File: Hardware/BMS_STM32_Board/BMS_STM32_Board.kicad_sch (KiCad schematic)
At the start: 0 parts

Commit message: hardware schematic
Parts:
- added C1, C2, C3, C4: 100nF, symbol Device:C_Small
- added C5: 4.7uF, symbol Device:C_Small
- added U1: STM32F103C8Tx, Package_QFP:LQFP-48_7x7mm_P0.5mm, symbol MCU_ST_STM32F1:STM32F103C8Tx
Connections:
- new net: U1.23 (VSS), U1.35 (VSS), U1.47 (VSS)
- new net +3V3: C1.1, C2.1, C3.1, C4.1, C5.1
- new net GND: C1.2, C2.2, C3.2, C4.2, C5.2

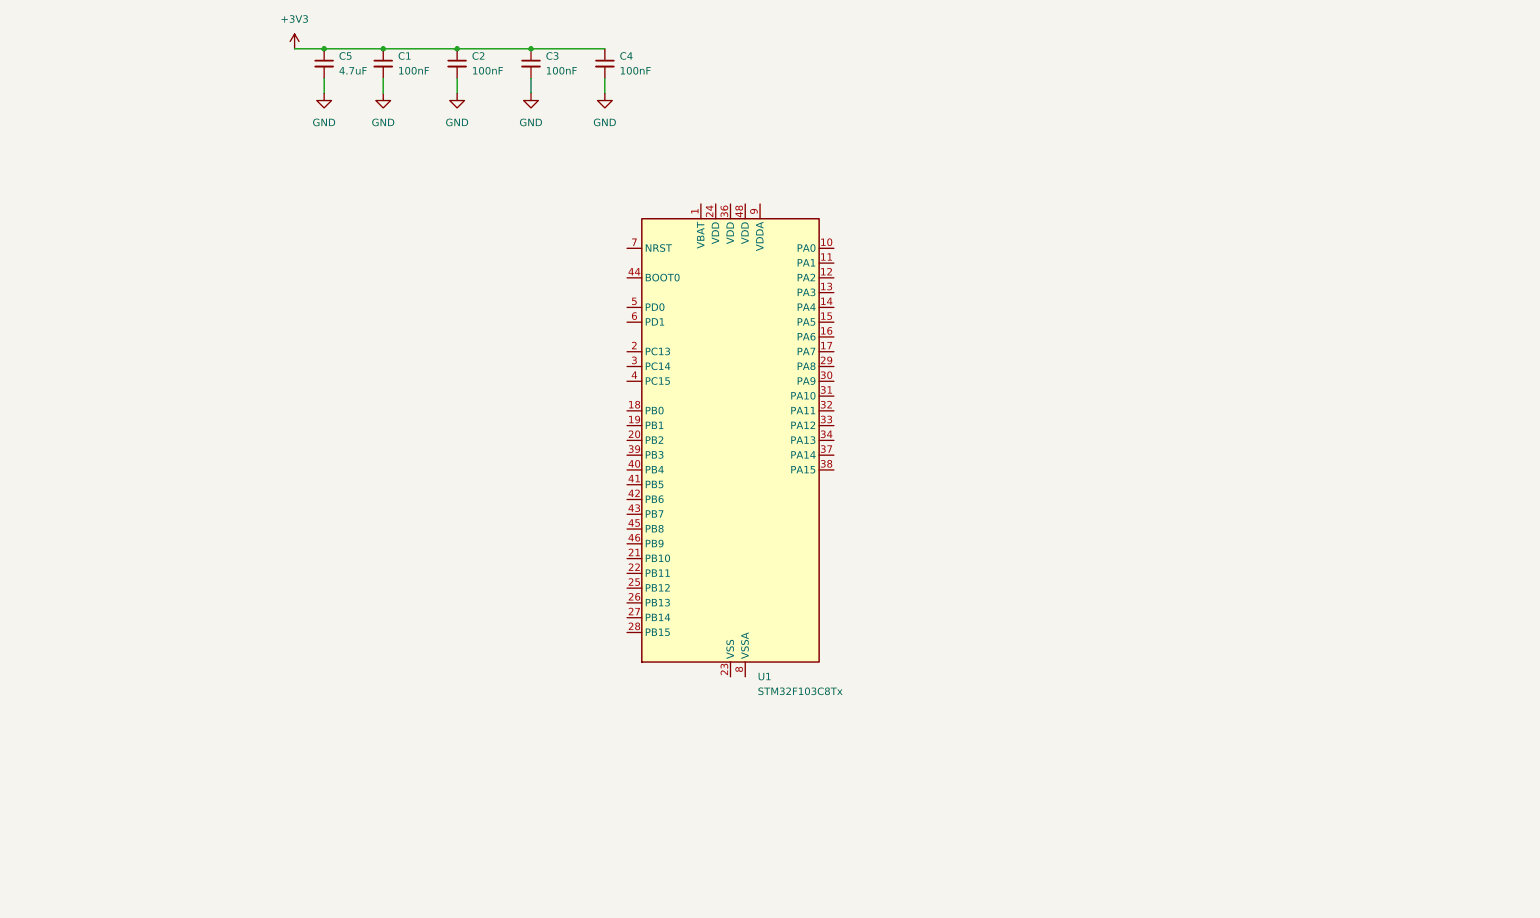
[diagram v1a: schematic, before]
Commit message: Current Sense Schematic
The current sense schematic was added the bms_stm32_board.
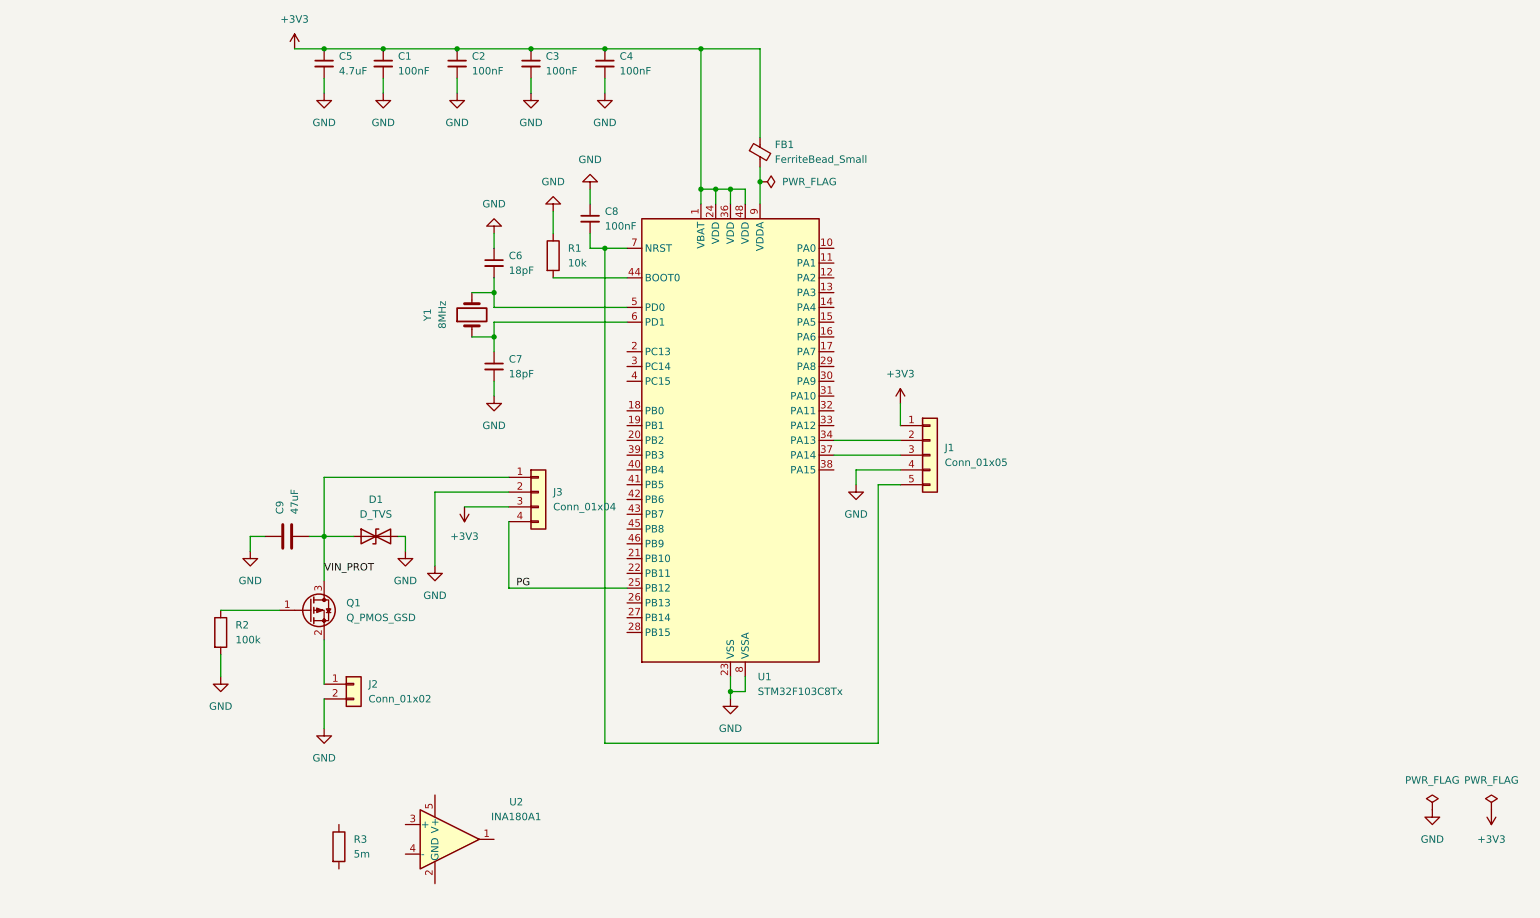
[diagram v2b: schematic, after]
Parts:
- added C6, C7: 18pF, symbol Device:C_Small
- added C8: 100nF, symbol Device:C_Small
- added C9: 47uF, symbol Device:C
- added D1: D_TVS, symbol Device:D_TVS
- added FB1: FerriteBead_Small, symbol Device:FerriteBead_Small
- added J1: Conn_01x05, symbol Connector_Generic:Conn_01x05
- added J2: Conn_01x02, symbol Connector_Generic:Conn_01x02
- added J3: Conn_01x04, symbol Connector_Generic:Conn_01x04
- added Q1: Q_PMOS_GSD, symbol Transistor_FET:Q_PMOS_GSD
- added R1: 10k, symbol Device:R
- added R2: 100k, symbol Device:R
- added R3: 5m, symbol Device:R
- added U2: INA180A1, Package_TO_SOT_SMD:SOT-23-5, symbol Amplifier_Current:INA180A1
- added Y1: 8MHz, symbol Device:Crystal
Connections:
- net +3V3: now also U1.1 (VBAT), U1.24 (VDD), U1.36 (VDD), U1.48 (VDD), FB1.1, J1.1 (Pin_1), J3.3 (Pin_3)
- net GND: now also U1.23 (VSS), U1.35 (VSS), U1.47 (VSS), U1.8 (VSSA), C6.1, C7.2, C8.1, C9.1, D1.2 (A2), J1.4 (Pin_4), J2.2 (Pin_2), J3.2 (Pin_2), R1.1, R2.2
- net PG: now reaches U1.25 (PB12)
- net PG: now also J3.4 (Pin_4)
- net at U1.34 (PA13): now also J1.2 (Pin_2)
- net at U1.37 (PA14): now also J1.3 (Pin_3)
- net at U1.44 (BOOT0): now also R1.2
- net at U1.5 (PD0): now also C6.2, Y1.2
- net at U1.6 (PD1): now also C7.1, Y1.1
- net at U1.7 (NRST): now also C8.2, J1.5 (Pin_5)
- net at U1.9 (VDDA): now also FB1.2
- new net: Q1.1 (G), R2.1
- new net: J2.1 (Pin_1), Q1.2 (S)
- new net VIN_PROT: C9.2, D1.1 (A1), J3.1 (Pin_1), Q1.3 (D)

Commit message: current sense
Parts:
- removed U2: INA180A1, Package_TO_SOT_SMD:SOT-23-5, symbol Amplifier_Current:INA180A1
- added C10, C11, C12: 100nF, symbol Device:C_Small
- added J4: Conn_01x02, symbol Connector_Generic:Conn_01x02
- added R4, R5: 10k, symbol Device:R
- added R6: 1k, symbol Device:R
- added U3: INA181, Package_TO_SOT_SMD:SOT-23-6, symbol Amplifier_Current:INA181
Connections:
- net +3V3: now also C10.1, R5.1, U3.6 (V+)
- net GND: now also C10.2, C11.1, C12.2, J4.2 (Pin_2), R4.2, U3.2 (GND)
- net VIN_PROT: now also R3.2, U3.4 (-)
- net LOAD+: now reaches R3.1
- net LOAD+: now also J4.1 (Pin_1), U3.3 (+)
- net at U1.18 (PB0): now also C11.2, R6.1
- new net: C12.1, R4.1, R5.2, U3.5 (REF)
- new net: R6.2, U3.1
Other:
- moved on the sheet: C6, C7, R1, R3, Y1

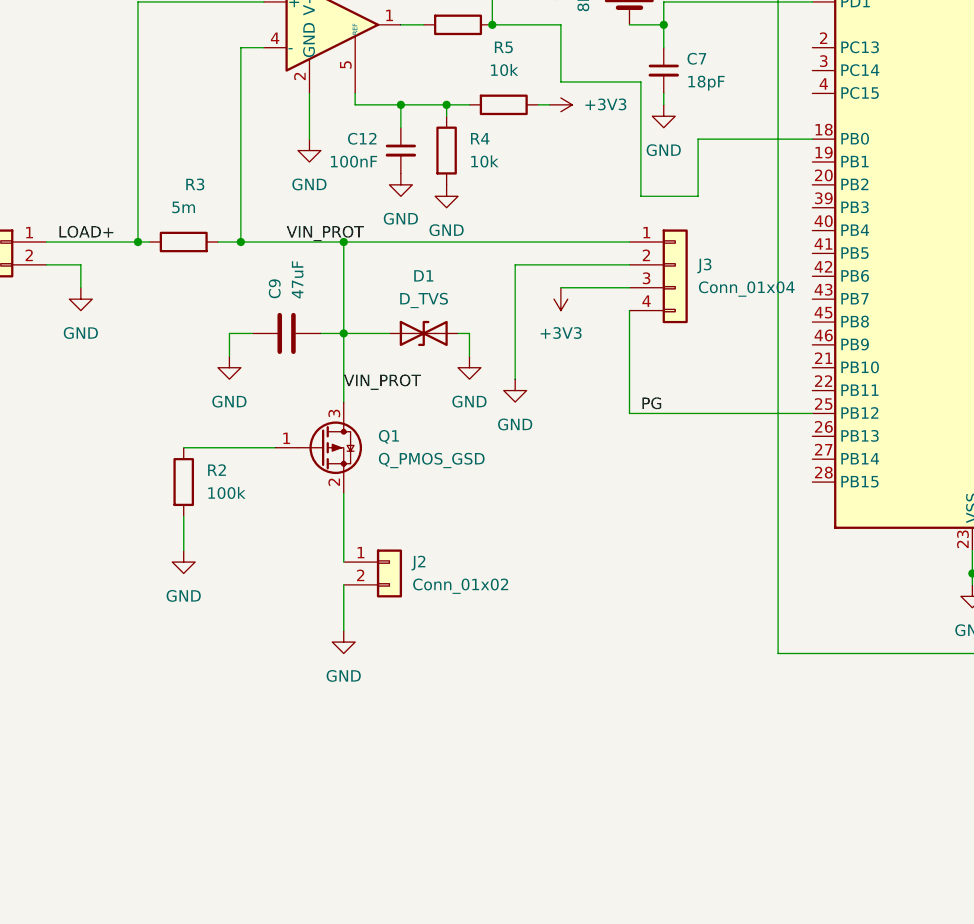
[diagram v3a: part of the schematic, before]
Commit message: Hardware: voltage sense divider (33k/10k + 100nF) to PB1, ERC clean
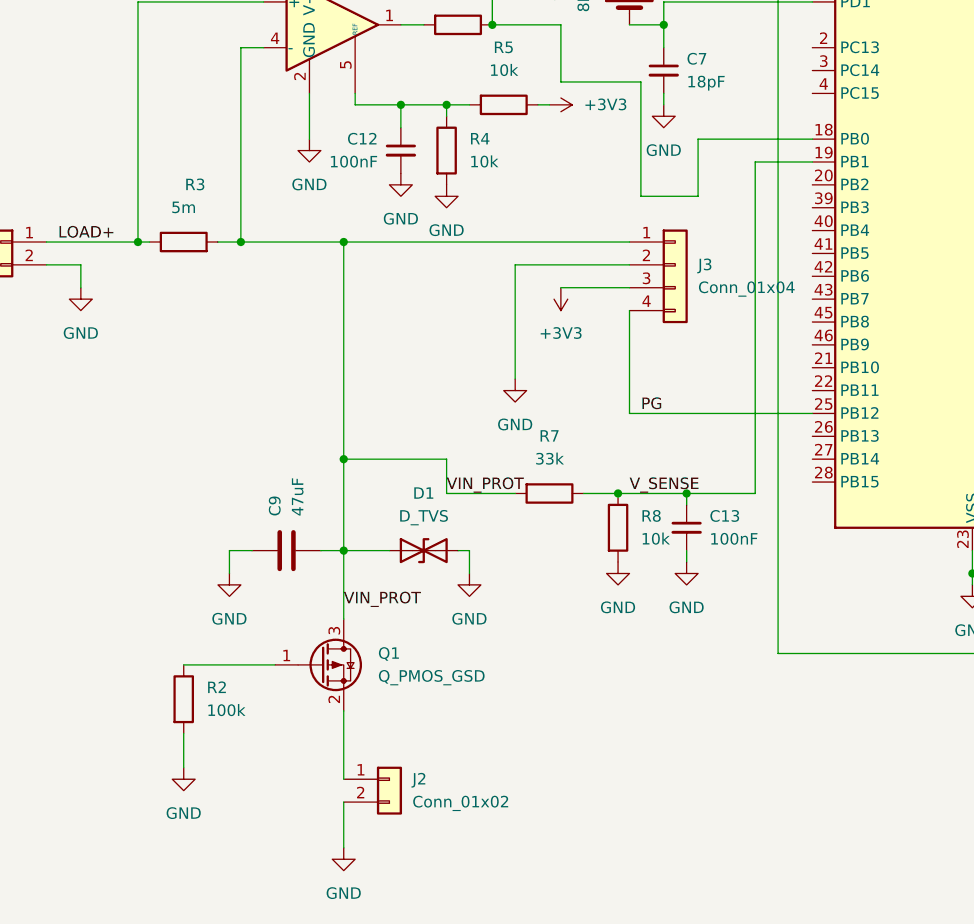
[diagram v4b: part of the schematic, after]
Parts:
- added C13: 100nF, symbol Device:C_Small
- added R7: 33k, symbol Device:R
- added R8: 10k, symbol Device:R
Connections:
- net GND: now also C13.2, R8.2
- net VIN_PROT: now also R7.2
- net V_SENSE: now reaches U1.19 (PB1)
- net V_SENSE: now also C13.1, R7.1, R8.1
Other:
- moved on the sheet: C9, D1, J2, Q1, R2

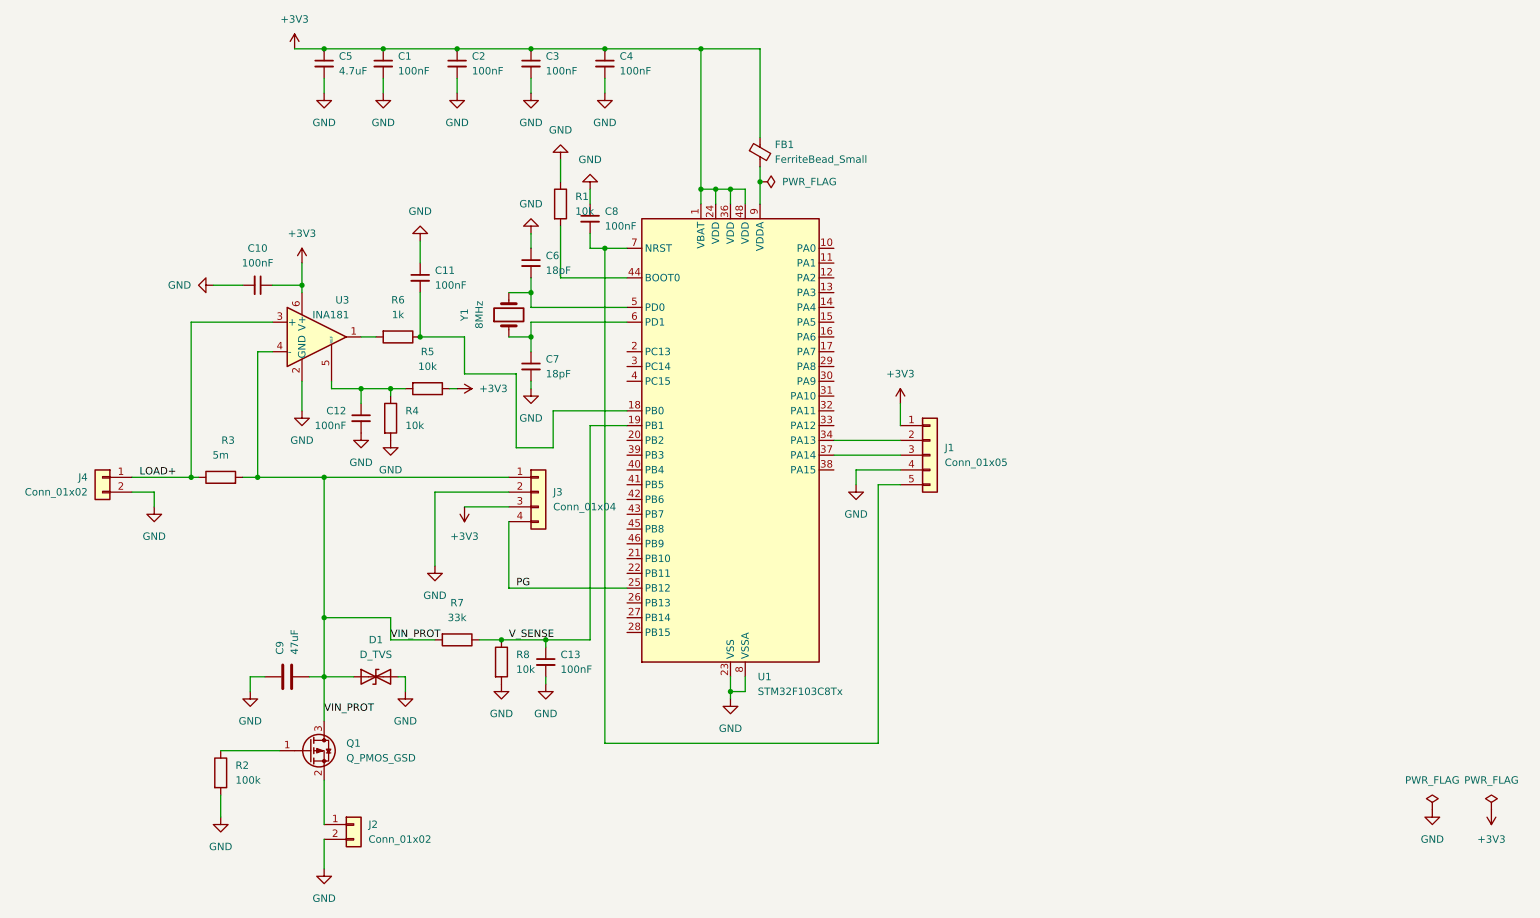
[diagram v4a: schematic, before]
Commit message: Hardware: TM1637 display block + LED indicators, ERC clean
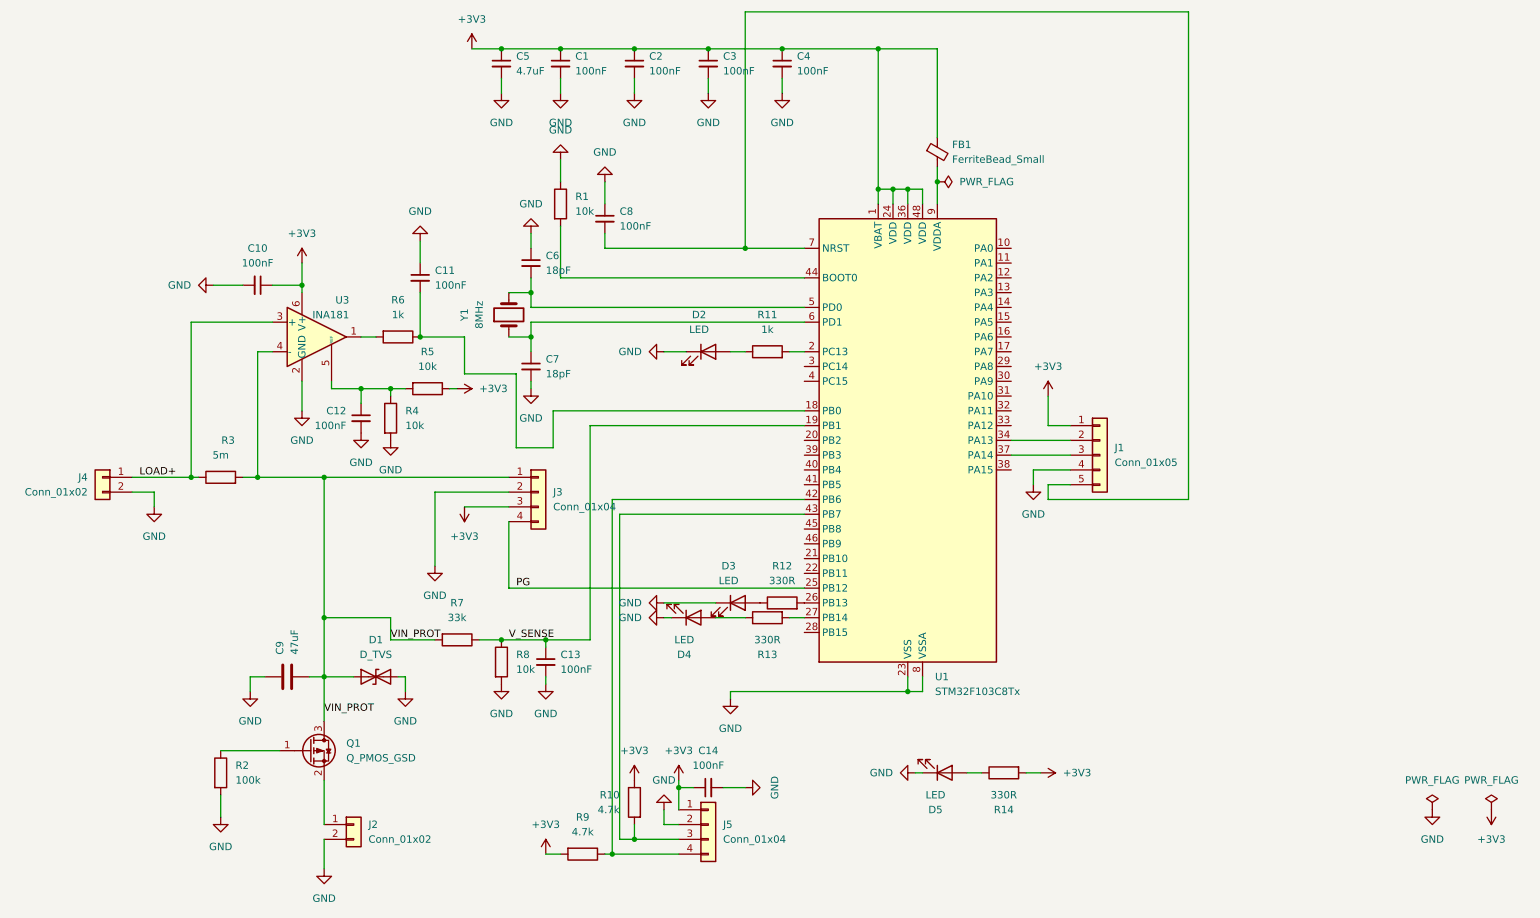
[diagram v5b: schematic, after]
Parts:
- added C14: 100nF, symbol Device:C_Small
- added D2, D3, D4, D5: LED, symbol Device:LED
- added J5: Conn_01x04, symbol Connector_Generic:Conn_01x04
- added R10, R9: 4.7k, symbol Device:R
- added R11: 1k, symbol Device:R
- added R12, R13, R14: 330R, symbol Device:R
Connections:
- net +3V3: now also C14.1, J5.1 (Pin_1), R10.1, R14.2, R9.2
- net GND: now also C14.2, D2.1 (K), D3.1 (K), D4.1 (K), D5.1 (K), J5.2 (Pin_2)
- net at U1.2 (PC13): now also R11.2
- net at U1.26 (PB13): now also R12.2
- net at U1.27 (PB14): now also R13.2
- net at U1.42 (PB6): now also J5.4 (Pin_4), R9.1
- net at U1.43 (PB7): now also J5.3 (Pin_3), R10.2
- new net: D2.2 (A), R11.1
- new net: D5.2 (A), R14.1
- new net: D3.2 (A), R12.1
- new net: D4.2 (A), R13.1
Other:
- moved on the sheet: C1, C2, C3, C4, C5, C8, FB1, J1, U1

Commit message: Hardware: thermistor footprint (DNP), schematic complete — ERC clean
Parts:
- added C15: 100nF, symbol Device:C_Small
- added R15: 10k, symbol Device:R
- added TH1: Thermistor_NTC, symbol Device:Thermistor_NTC
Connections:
- net +3V3: now also R15.1
- net GND: now also C15.2, TH1.2
- net T_SENSE: now reaches U1.10 (PA0)
- net T_SENSE: now also C15.1, R15.2, TH1.1
- no-connect marks 0 -> 24
